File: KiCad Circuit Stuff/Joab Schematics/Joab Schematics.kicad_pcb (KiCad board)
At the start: 2 copper layers, 44 parts, among them Q1 MMBT3904, Q2 S8550, U1 MT3608, U2 AMS1117-3.3, U3 MCP73831-2-OT, U5 TPS5430DDA

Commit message: Added INA219 monitor (kinda) and added some fixes
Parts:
- added C11: 0.1u, Capacitor_SMD:C_0402_1005Metric_Pad0.74x0.62mm_HandSolder, F.Cu at (180.8, 71.6)
- added J1: Conn_02x16_Odd_Even, Connector_PinHeader_2.54mm:PinHeader_2x16_P2.54mm_Vertical, F.Cu at (178.8, 143.8)
- added J2: Conn_01x02, Connector_JST:JST_PH_B2B-PH-K_1x02_P2.00mm_Vertical, F.Cu at (203.3, 76.3)
- added JP1: Possible Filter Cap, Jumper:SolderJumper-2_P1.3mm_Open_Pad1.0x1.5mm, F.Cu at (153.9, 66.3)
- added JP2: Possible Filter Res2, Jumper:SolderJumper-2_P1.3mm_Open_Pad1.0x1.5mm, F.Cu at (153.9, 69.8)
- added JP3: Possible Filter Res1, Jumper:SolderJumper-2_P1.3mm_Open_Pad1.0x1.5mm, F.Cu at (153.9, 73.4)
- added R10: 0R, Resistor_SMD:R_0402_1005Metric_Pad0.72x0.64mm_HandSolder, F.Cu at (157.7, 65.5)
- added R11: 0R, Resistor_SMD:R_0402_1005Metric_Pad0.72x0.64mm_HandSolder, F.Cu at (157.7, 67.5)
- added R12: 0.1R, Resistor_SMD:R_0402_1005Metric_Pad0.72x0.64mm_HandSolder, F.Cu at (157.7, 69.5)
- added U4: INA219AxDCN, Package_TO_SOT_SMD:SOT-23-8, F.Cu at (176.6, 72.8)
- added U6: INA219BxDCN, Package_TO_SOT_SMD:SOT-23-8, F.Cu at (176.6, 77.3)
- L1: footprint Inductor_SMD:L_0402_1005Metric_Pad0.77x0.64mm_HandSolder -> Inductor_SMD:L_Changjiang_FNR4030S
- L2: value L_Small -> 47u; footprint Inductor_SMD:L_0402_1005Metric_Pad0.77x0.64mm_HandSolder -> Inductor_SMD:L_Sunlord_SWPA5040S
- Q2: footprint Package_TO_SOT_THT:TO-92_Inline -> Package_TO_SOT_SMD:SOT-23
- moved L1 20.8 mm to (139.5, 118.0)
- moved Q2 11.5 mm to (130.0, 100.2)
- moved Q1 11.1 mm to (132.2, 111.3)
- moved L2 9.31 mm to (138.8, 104.0)
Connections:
- C10 pad 2: /Battery -> /Battery_Out
- C2 pad 1: /Battery -> /Battery_Out
- L1 pad 1: /Battery -> /Battery_Out
- TP2 pad 1: /Battery -> /Battery_Out
- TP9 pad 1: /Battery -> /Battery_Out
- U1 pad 4: /Battery -> /Battery_Out
- U1 pad 5: /Battery -> /Battery_Out
- U3 pad 3: /Battery -> /Battery_Out

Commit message: Chaned Charrging IC, Chaned INA219 IC, Changed some other things
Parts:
- removed U6: INA219BxDCN, Package_TO_SOT_SMD:SOT-23-8
- C10, C9: value 4.7u -> 10u
- D1, D2: value SS34 -> SS34_C8678; footprint Diode_SMD:D_SMA_Handsoldering -> JLCPCB:SMA_L4.3-W2.6-LS5.2-RD
- R7: value 1.8k -> 2k
- R8: value 5k -> 5.5k
- TP1, TP10, TP11, TP12, TP13, TP14, TP15, TP2, TP3, TP4, TP5, TP6, TP7, TP8, TP9: footprint TestPoint:TestPoint_2Pads_Pitch2.54mm_Drill0.8mm -> TestPoint:TestPoint_Pad_2.5x2.5mm
- U3: value MCP73831-2-OT -> TP4056; footprint Package_TO_SOT_SMD:SOT-23-5 -> JLCPCB:ESOP-8_L4.9-W3.9-P1.27-LS6.0-BL-EP
- U4: value INA219AxDCN -> INA219AIDCNR; footprint Package_TO_SOT_SMD:SOT-23-8 -> JLCPCB:SOT-23-8_L3.0-W1.7-P0.65-LS2.8-BR
- moved J1 78.7 mm to (146.2, 72.1), turned to 0 degrees
- moved J2 40.6 mm to (167.0, 94.4)
- moved Q2 36.7 mm to (166.4, 104.9)
- moved Q1 35.9 mm to (166.4, 100.4)
- moved C1 35.3 mm to (175.5, 70.7)
- moved C10 35.3 mm to (178.7, 76.6)
- moved C2 35.3 mm to (175.5, 72.7)
- moved C3 35.3 mm to (175.5, 74.7)
- moved C4 35.3 mm to (175.5, 76.6)
- moved C5 35.3 mm to (175.5, 78.6)
- moved C6 35.3 mm to (175.5, 80.6)
- moved C7 35.3 mm to (178.7, 70.7)
- moved C8 35.3 mm to (178.7, 72.7)
- moved C9 35.3 mm to (178.7, 74.7)
- moved L1 33.8 mm to (171.7, 107.6)
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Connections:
- C1 pad 1: +5V -> Net-(C1-Pad1)
- TP4 pad 1: +5V -> Net-(C1-Pad1)
- U3 pad 1: unconnected-(U3-STAT-Pad1) -> GND
- U3 pad 2: GND -> Net-(Q2-C)
- U3 pad 3: /Battery_Out -> GND
- U3 pad 5: Net-(Q2-C) -> /Battery_Out
- U4 pad 1: unconnected-(U4-IN+-Pad1) -> Net-(JP1-B)
- U4 pad 2: unconnected-(U4-IN--Pad2) -> Net-(JP1-A)
- U4 pad 3: unconnected-(U4-GND-Pad3) -> GND
- U4 pad 4: unconnected-(U4-VS-Pad4) -> +3V3
- U4 pad 5: unconnected-(U4-SCL-Pad5) -> /I2C1_SCL
- U4 pad 6: unconnected-(U4-SDA-Pad6) -> /I2C1_SDA
- U4 pad 7: unconnected-(U4-A0-Pad7) -> GND
- U4 pad 8: unconnected-(U4-A1-Pad8) -> +3V3

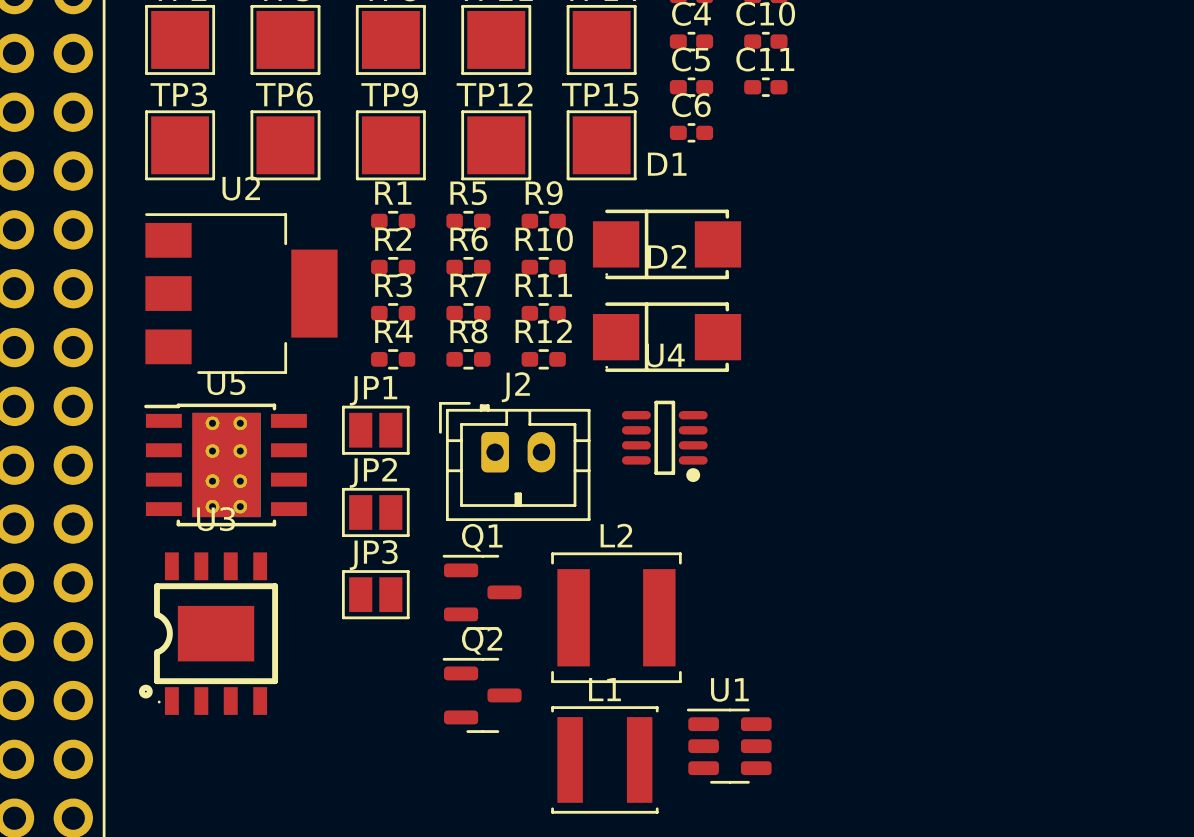
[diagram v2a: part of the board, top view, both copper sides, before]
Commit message: Added Switching for charger
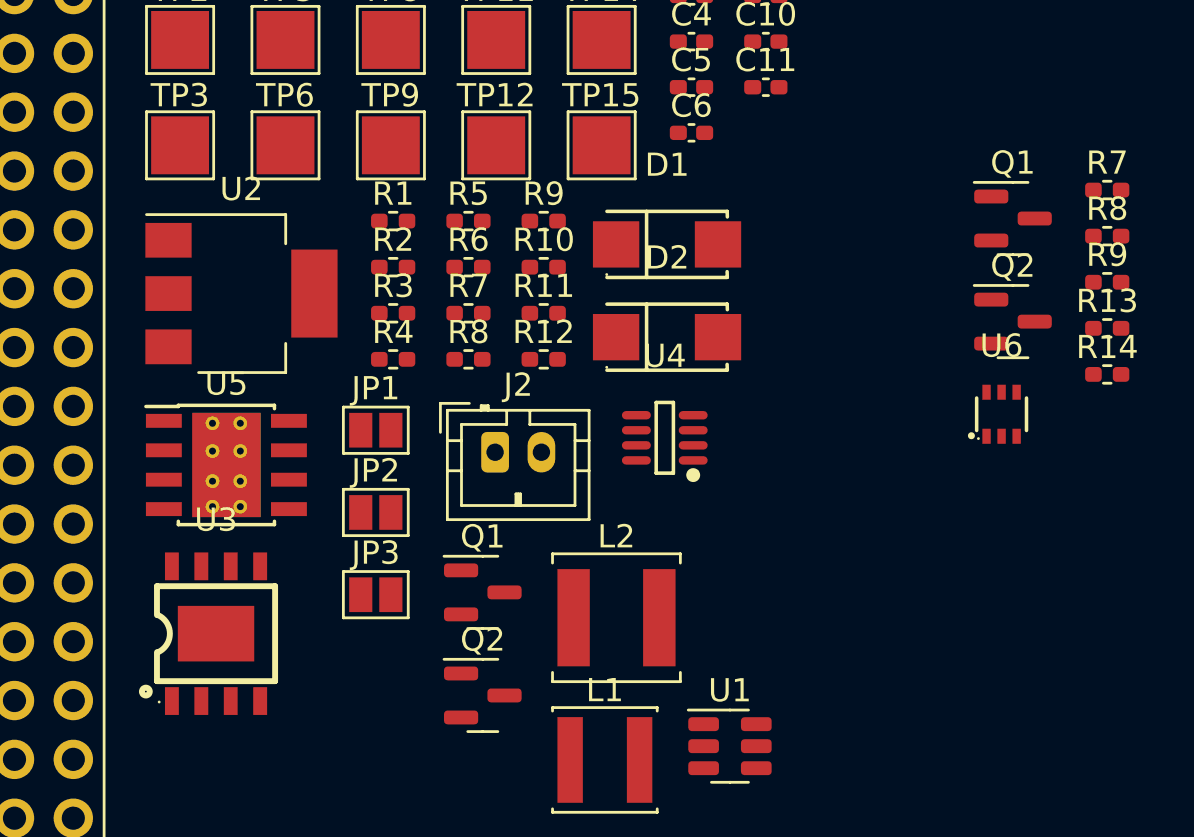
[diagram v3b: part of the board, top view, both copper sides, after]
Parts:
- added Q1: S8550, Package_TO_SOT_SMD:SOT-23, F.Cu at (189.3, 84.3)
- added Q2: MMBT3904, Package_TO_SOT_SMD:SOT-23, F.Cu at (189.3, 88.7)
- added R13: 2k, Resistor_SMD:R_0402_1005Metric_Pad0.72x0.64mm_HandSolder, F.Cu at (193.4, 89.0)
- added R14: 5.5k, Resistor_SMD:R_0402_1005Metric_Pad0.72x0.64mm_HandSolder, F.Cu at (193.4, 91.0)
- added R7: 5.5k, Resistor_SMD:R_0402_1005Metric_Pad0.72x0.64mm_HandSolder, F.Cu at (193.4, 83.0)
- added R8: 2k, Resistor_SMD:R_0402_1005Metric_Pad0.72x0.64mm_HandSolder, F.Cu at (193.4, 85.0)
- added R9: 1000k, Resistor_SMD:R_0402_1005Metric_Pad0.72x0.64mm_HandSolder, F.Cu at (193.4, 87.0)
- added U6: TS5A3159DCKR, JLCPCB:SC-70-6_L2.0-W1.3-P0.65-LS2.1-BL-1, F.Cu at (188.8, 92.7)
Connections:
- U3 pad 2: Net-(Q2-C) -> Net-(U3-PROG)

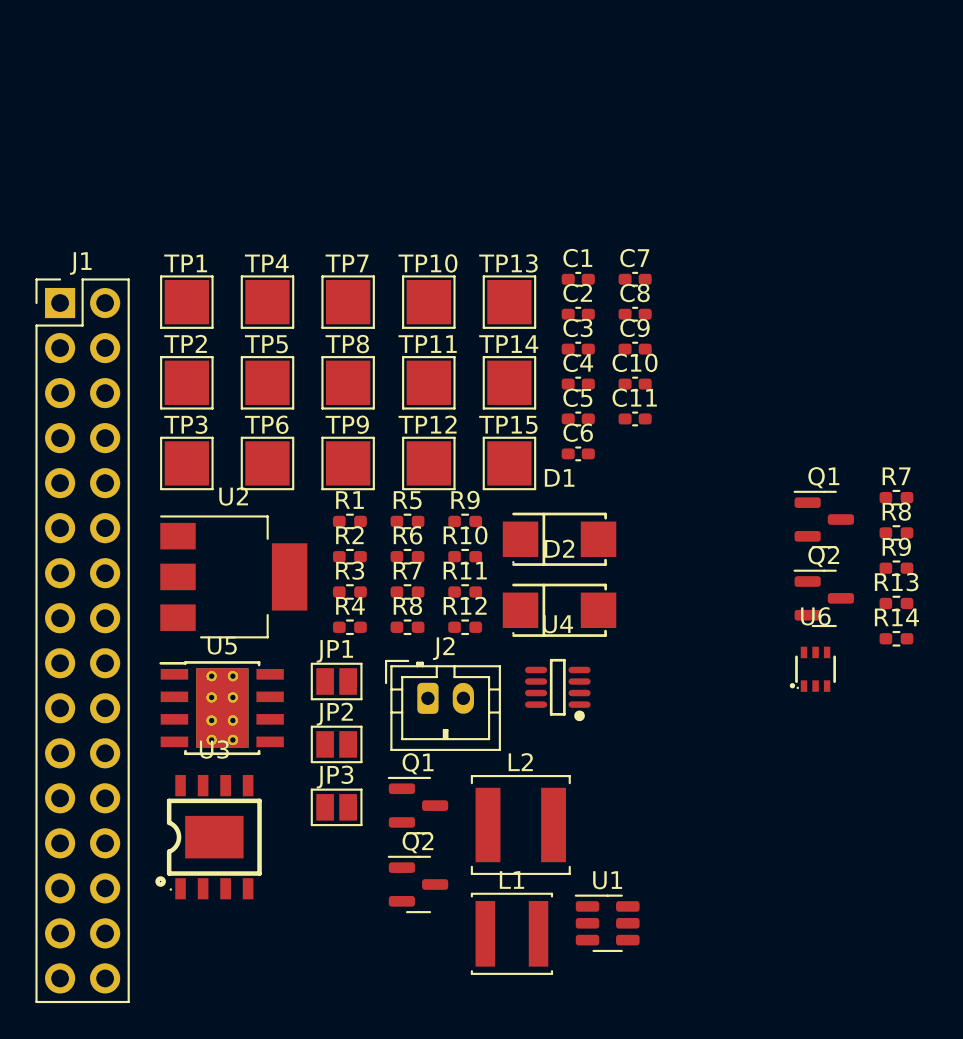
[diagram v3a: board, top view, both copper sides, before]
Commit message: Changed some values of resistors, caps and inductors, Also modified some components Still need to finish adding resistors from jlcpcb
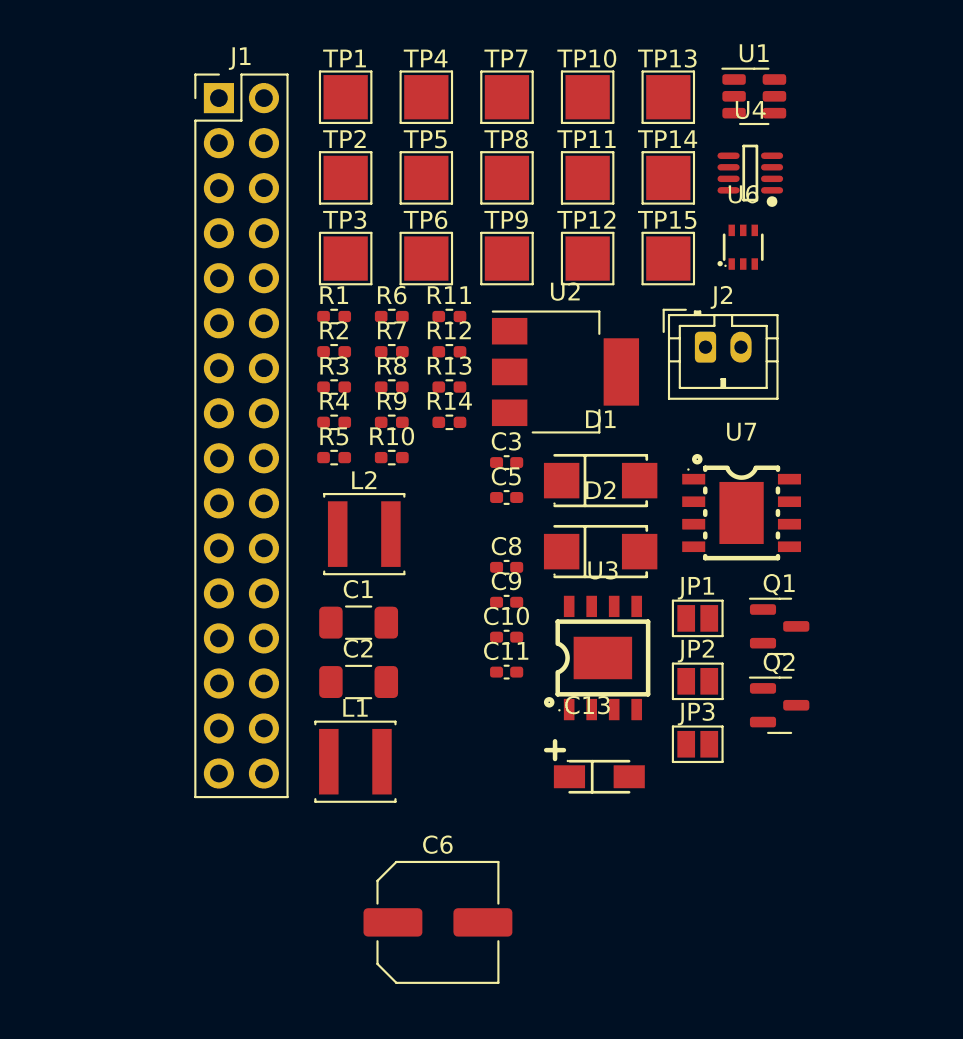
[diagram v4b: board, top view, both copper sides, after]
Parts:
- removed C4: 10u, Capacitor_SMD:C_0402_1005Metric_Pad0.74x0.62mm_HandSolder
- removed C7: 4.7u, Capacitor_SMD:C_0402_1005Metric_Pad0.74x0.62mm_HandSolder
- removed the Q1 at (166.4, 100.4)
- removed the Q1 at (189.3, 84.3)
- removed the Q2 at (166.4, 104.9)
- removed the Q2 at (189.3, 88.7)
- removed the R7 at (165.8, 88.4)
- removed the R7 at (193.4, 83.0)
- removed the R8 at (165.8, 90.3)
- removed the R8 at (193.4, 85.0)
- removed the R9 at (193.4, 87.0)
- removed the R9 at (169.1, 84.4)
- removed U5: TPS5430DDA, Package_SO:TI_SO-PowerPAD-8_ThermalVias
- added C13: TAJA106K016RNJ, JLCPCB:CAP-SMD_L3.2-W1.6-RD-C7171, F.Cu at (176.6, 98.8)
- added Q1: S8550, Package_TO_SOT_SMD:SOT-23, F.Cu at (186.8, 90.3)
- added Q2: MMBT3904, Package_TO_SOT_SMD:SOT-23, F.Cu at (186.8, 94.8)
- added R7: 5.5k, Resistor_SMD:R_0402_1005Metric_Pad0.72x0.64mm_HandSolder, F.Cu at (164.9, 74.8)
- added R8: 2k, Resistor_SMD:R_0402_1005Metric_Pad0.72x0.64mm_HandSolder, F.Cu at (164.9, 76.8)
- added R9: 1000k, Resistor_SMD:R_0402_1005Metric_Pad0.72x0.64mm_HandSolder, F.Cu at (164.9, 78.8)
- added U7: TPS5430DDAR, JLCPCB:ESOP-8_L4.9-W3.9-P1.27-LS6.0-TL-EP, F.Cu at (184.7, 83.9)
- C1, C2: footprint Capacitor_SMD:C_0402_1005Metric_Pad0.74x0.62mm_HandSolder -> Capacitor_SMD:C_1206_3216Metric_Pad1.33x1.80mm_HandSolder
- C6: footprint Capacitor_SMD:C_0402_1005Metric_Pad0.74x0.62mm_HandSolder -> Capacitor_SMD:C_Elec_6.3x7.7
- L2: value 47u -> 18u; footprint Inductor_SMD:L_Sunlord_SWPA5040S -> Inductor_SMD:L_Changjiang_FNR4030S
- moved U1 47.4 mm to (185.4, 60.4)
- moved U4 31.0 mm to (185.2, 64.7)
- moved R13 28.0 mm to (168.2, 76.8)
- moved R14 28.0 mm to (168.2, 78.8)
- moved C6 27.6 mm to (167.5, 107.0)
- moved J2 25.3 mm to (182.6, 74.5)
- moved C2 24.2 mm to (163.1, 93.4)
- moved U6 24.2 mm to (184.8, 68.9)
- moved U3 24.1 mm to (176.8, 92.1)
- moved C1 23.0 mm to (163.1, 90.1)
- moved U2 22.0 mm to (174.7, 76.0)
- moved JP1 20.7 mm to (182.2, 89.8)
- moved JP3 20.7 mm to (182.2, 97.0)
- moved JP2 20.7 mm to (182.2, 93.4)
- moved L2 18.6 mm to (163.4, 85.1)
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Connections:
- net Net-(D2-K) renamed /PH_Pin
- C1 pad 1: Net-(C1-Pad1) -> +5V
- TP4 pad 1: Net-(C1-Pad1) -> +5V
